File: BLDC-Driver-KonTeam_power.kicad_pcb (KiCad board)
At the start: 2 copper layers, 170 x 98.5 mm, 66 parts, among them J1 HOA_Enable, J10 HOB_Enable, J11 LOB_Enable, J12 A, J13 B, J14 C, J2 BUck, J3 Logic_Conn, J4 Logic_Test, J6 IN, J7 LOC_Enable, J8 HOC_Enable, J9 LOA_Enable, Q1 IRFZ44N, Q11 IRFZ44N, Q3 IRFZ44N, Q5 IRFZ44N, Q7 IRFZ44N, Q9 IRFZ44N, U1 IR2101, U2 IR2101, U3 IR2101, U4 LM7805_TO220

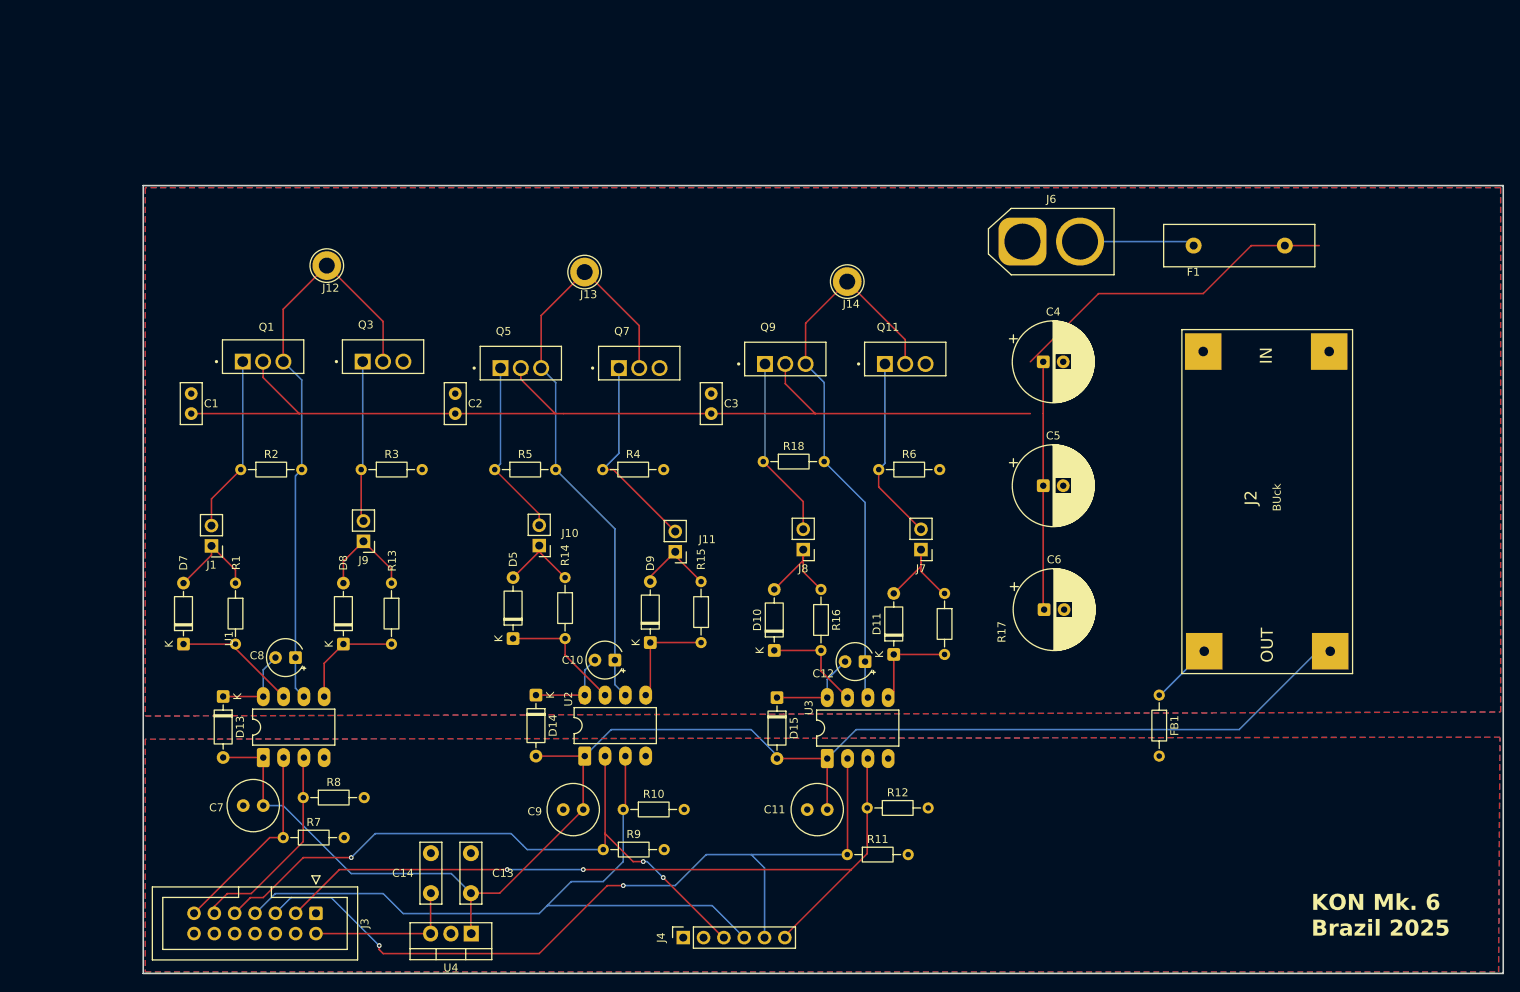
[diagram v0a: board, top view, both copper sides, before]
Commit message: - Added Footprint Buck converter - Add TVS diode for over voltage protection - Routed tracks (need confirmation) - Add conector for the horn, need to add specific connector - Added .step format for the mecanical considerations
Todo:
- add holes to fix to the car structure
- Make specific connector for the horn
- Calculate heatsink spacing
- Investigate about RC snubbers
- Investigate about the fly back diode efficency in the new mosfet
- Make the proyect has the embebed libraries for buck converter, mosfets, 
- Add Documentation Folder. (Datasheets, comparation sheets , etc)
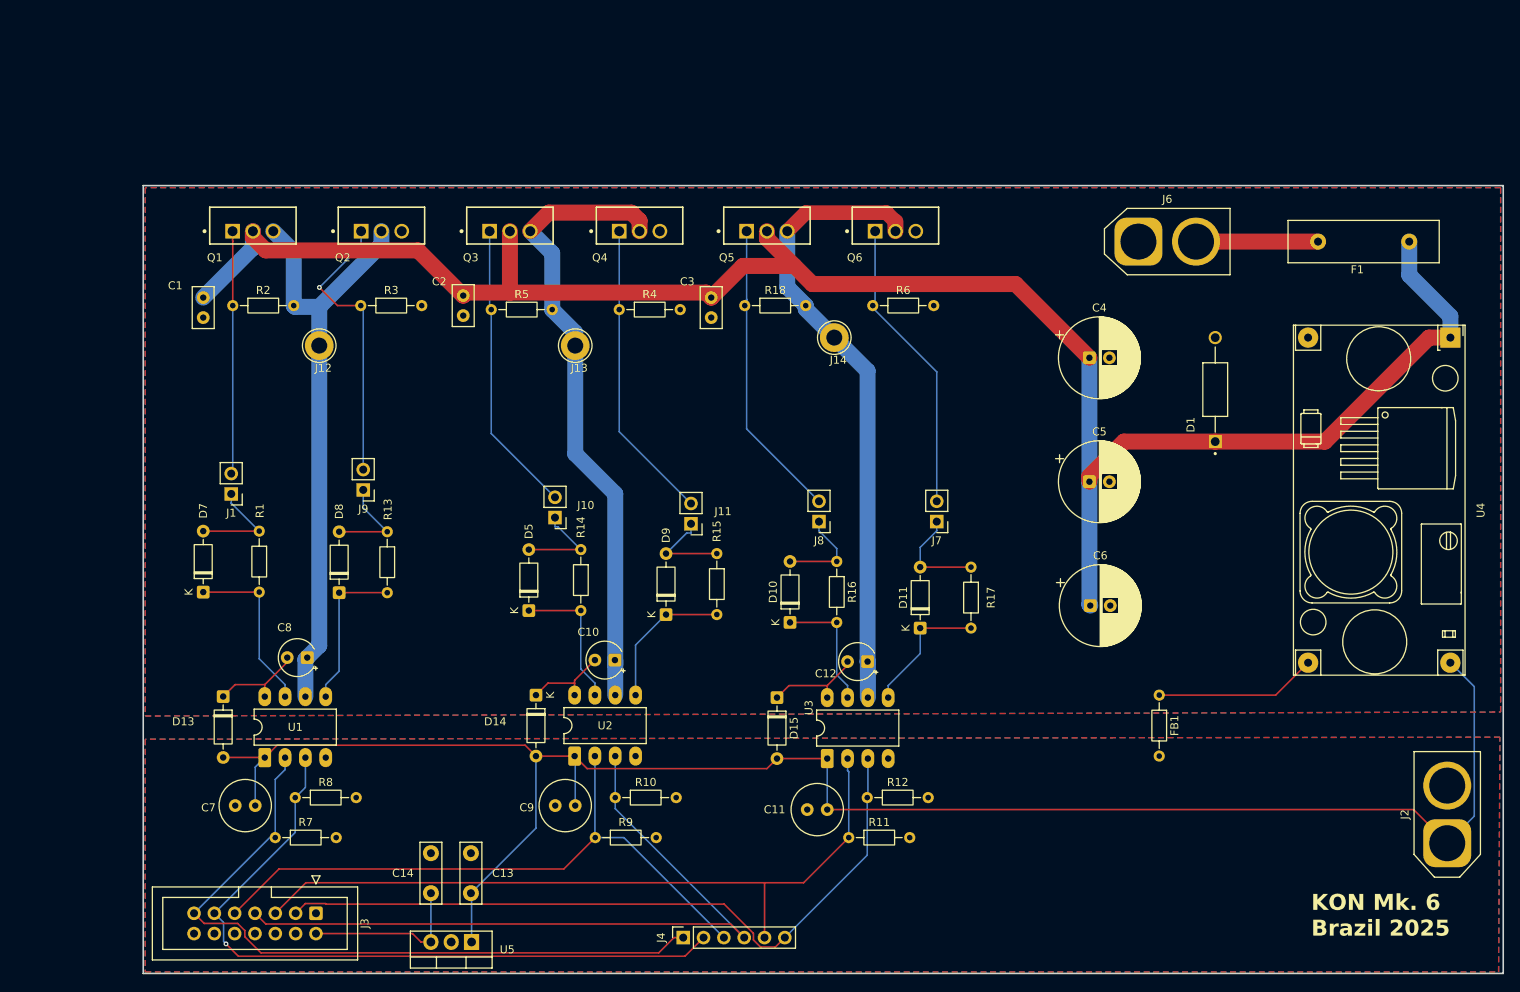
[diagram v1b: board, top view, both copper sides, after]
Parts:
- removed Q11, Q7, Q9: IRFZ44N, IRFZ44N:TO254P1016X419X2286-3
- added D1: P6KE68A, P6KE68A:DIOAD1300W80L670D310, F.Cu at (194.0, 72.0)
- added Q2: IRFB7730, kicad:IRFB7730, F.Cu at (89.8, 52.2)
- added Q4: IRFB7730, kicad:IRFB7730, F.Cu at (122.0, 52.2)
- added Q6: IRFB7730, kicad:IRFB7730, F.Cu at (154.0, 52.2)
- added U5: LM7805_TO220, Package_TO_SOT_THT:TO-220-3_Vertical, F.Cu at (101.0, 141.1)
- FB1: value FerriteBead_Small -> FerriteBead
- J2: value BUck -> Horn; footprint DC_DC_LM2596_small:DC_DC_LM2596_small -> Connector_AMASS:AMASS_XT60-F_1x02_P7.20mm_Vertical
- Q1, Q3, Q5: value IRFZ44N -> IRFB7730; footprint IRFZ44N:TO254P1016X419X2286-3 -> kicad:IRFB7730
- U4: value LM7805_TO220 -> Buck Converter; footprint Package_TO_SOT_THT:TO-220-3_Vertical -> KiCad:YAAJ_DCDC_StepDown_LM2596
- moved U4 143.3 mm to (223.4, 65.5), turned to -90 degrees
- moved J2 49.0 mm to (223.0, 128.7), turned to 90 degrees
- moved Q5 35.2 mm to (138.0, 52.2), turned to 90 degrees
- moved Q3 22.7 mm to (105.8, 52.2), turned to 90 degrees
- moved R2 20.5 mm to (71.2, 61.5)
- moved R6 20.5 mm to (151.2, 61.5)
- moved R3 20.5 mm to (87.2, 61.5)
- moved R4 20.1 mm to (119.5, 62.0)
- moved R5 20.0 mm to (103.5, 62.0)
- moved R18 19.6 mm to (135.2, 61.5)
- moved Q1 16.3 mm to (73.7, 52.2), turned to 90 degrees
- moved F1 15.6 mm to (218.2, 53.5)
- moved J6 14.5 mm to (184.4, 53.5)
- moved J12 10.0 mm to (82.0, 66.5)
- moved C2 9.80 mm to (100.0, 62.8), turned to 90 degrees
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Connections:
- net Net-(J6-Pin_2) renamed /Vin
- FB1 pad 1: Net-(J2-Pin_4) -> Net-(FB1-Pad1)
- J2 pad 1: VCC -> +12V
- J2 pad 2: GND -> Earth
- Q3 pad 1: LO_A -> HO_B
- Q3 pad 2: MA -> VCC
- Q3 pad 3: GND -> MB
- Q5 pad 1: HO_B -> HO_C
- Q5 pad 3: MB -> MC
- U4 pad 1: +12V -> VCC
- U4 pad 2: Earth -> GND
- U4 pad 3: +5V -> Net-(FB1-Pad1)
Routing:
- net /LIN_A: track 25.9 -> 89.9 mm, vias 0 -> 1
- net /HIN_A: track 25.1 -> 89.0 mm
- net +12V: track 185.1 -> 228.1 mm
- net VCC: track 204.4 -> 237.6 mm
- net Net-(FB1-Pad1): track 0.00 -> 20.3 mm
- net LO_A: track 20.1 -> 35.9 mm, vias 0 -> 1
- net HO_C: track 22.8 -> 38.4 mm
- net LO_C: track 23.2 -> 37.7 mm
- net HO_B: track 22.3 -> 36.6 mm
- net LO_B: track 25.8 -> 37.8 mm
- net /HIN_C: track 103.7 -> 92.4 mm, vias 2 -> 0
- net HO_A: track 22.1 -> 30.4 mm
- net MC: track 70.7 -> 78.6 mm
- net Net-(J2-Pin_4): track 7.90 -> 0.00 mm
- net /LIN_C: track 98.4 -> 91.6 mm, vias 2 -> 0
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
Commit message: cambio de driver, cambio de mosfet , añadido aislamiento galvanico entre logica y potencia
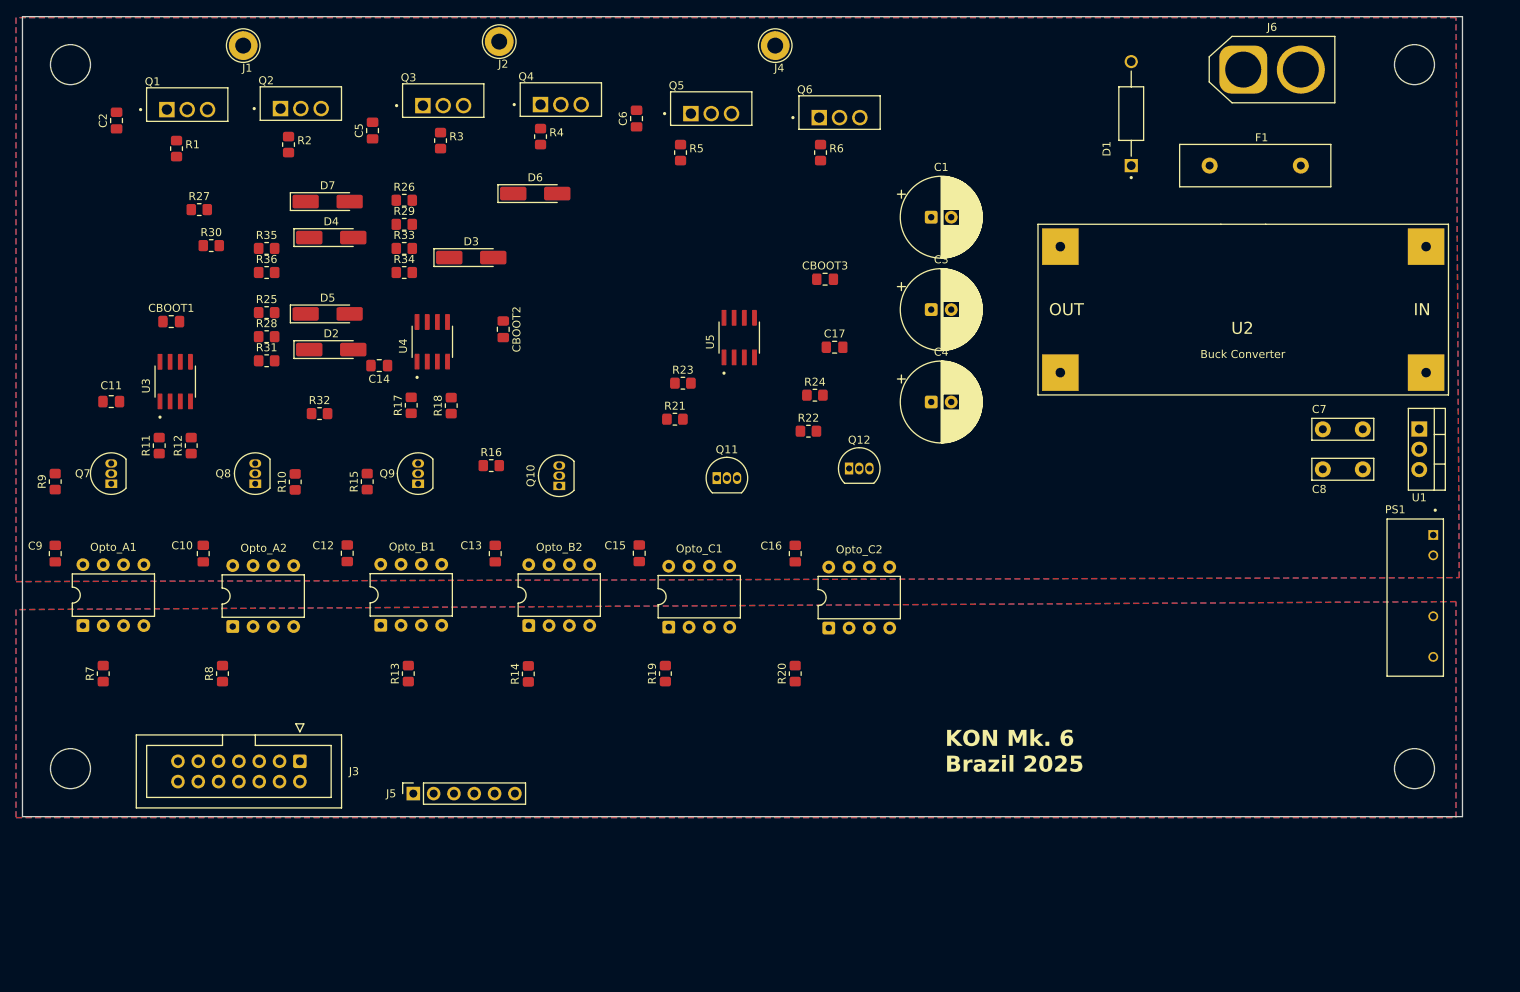
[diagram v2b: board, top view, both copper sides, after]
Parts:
- removed D10, D11, D13, D14, D15, D8, D9: SR560, Diode_THT:D_DO-35_SOD27_P7.62mm_Horizontal
- removed FB1: FerriteBead, Resistor_THT:R_Axial_DIN0204_L3.6mm_D1.6mm_P7.62mm_Horizontal
- removed J10: HOB_Enable, Connector_PinHeader_2.54mm:PinHeader_1x02_P2.54mm_Vertical
- removed J11: LOB_Enable, Connector_PinHeader_2.54mm:PinHeader_1x02_P2.54mm_Vertical
- removed J12: A, TestPoint:TestPoint_Loop_D3.80mm_Drill2.0mm
- removed J13: B, TestPoint:TestPoint_Loop_D3.80mm_Drill2.0mm
- removed J14: C, TestPoint:TestPoint_Loop_D3.80mm_Drill2.0mm
- removed J7: LOC_Enable, Connector_PinHeader_2.54mm:PinHeader_1x02_P2.54mm_Vertical
- removed J8: HOC_Enable, Connector_PinHeader_2.54mm:PinHeader_1x02_P2.54mm_Vertical
- removed J9: LOA_Enable, Connector_PinHeader_2.54mm:PinHeader_1x02_P2.54mm_Vertical
- added C15: 2.2uF, Capacitor_SMD:C_0805_2012Metric_Pad1.18x1.45mm_HandSolder, F.Cu at (122.0, 92.5)
- added C16: 2.2uF, Capacitor_SMD:C_0805_2012Metric_Pad1.18x1.45mm_HandSolder, F.Cu at (141.5, 92.5)
- added C17: 100uF, Capacitor_SMD:C_0805_2012Metric_Pad1.18x1.45mm_HandSolder, F.Cu at (146.4, 66.7)
- added CBOOT1: 6.8uF, Capacitor_SMD:C_0805_2012Metric_Pad1.18x1.45mm_HandSolder, F.Cu at (63.5, 63.5)
- added CBOOT2: 6.8uF, Capacitor_SMD:C_0805_2012Metric_Pad1.18x1.45mm_HandSolder, F.Cu at (105.0, 64.5)
- added CBOOT3: 6.8uF, Capacitor_SMD:C_0805_2012Metric_Pad1.18x1.45mm_HandSolder, F.Cu at (145.2, 58.2)
- added D2: LL4148, Diode_SMD:D_MiniMELF_Handsoldering, F.Cu at (83.5, 67.0)
- added D3: LL4148, Diode_SMD:D_MiniMELF_Handsoldering, F.Cu at (101.0, 55.5)
- added D4: LL4148, Diode_SMD:D_MiniMELF_Handsoldering, F.Cu at (83.5, 53.0)
- added D6: LL4148, Diode_SMD:D_MiniMELF_Handsoldering, F.Cu at (109.0, 47.5)
- added J5: Logic_Test, Connector_PinSocket_2.54mm:PinSocket_1x06_P2.54mm_Vertical, F.Cu at (93.8, 122.5)
- added Opto_A1: 6N137, Package_DIP:DIP-8_W7.62mm, F.Cu at (52.5, 101.5)
- added Opto_A2: 6N137, Package_DIP:DIP-8_W7.62mm, F.Cu at (71.2, 101.6)
- added Opto_B1: 6N137, Package_DIP:DIP-8_W7.62mm, F.Cu at (89.7, 101.5)
- added Opto_B2: 6N137, Package_DIP:DIP-8_W7.62mm, F.Cu at (108.2, 101.5)
- added Opto_C1: 6N137, Package_DIP:DIP-8_W7.62mm, F.Cu at (125.7, 101.7)
- added Opto_C2: 6N137, Package_DIP:DIP-8_W7.62mm, F.Cu at (145.7, 101.8)
- added PS1: RKZE-1205S_HP, KON:CONV_RKZE-1205S_HP, F.Cu at (219.0, 98.0)
- added Q10: 2N7000, Package_TO_SOT_THT:TO-92_Inline, F.Cu at (112.0, 84.0)
- added Q11: 2N7000, Package_TO_SOT_THT:TO-92_Inline, F.Cu at (131.7, 83.1)
- added Q12: 2N7000, Package_TO_SOT_THT:TO-92_Inline, F.Cu at (148.2, 81.9)
- added Q7: 2N7000, Package_TO_SOT_THT:TO-92_Inline, F.Cu at (56.0, 83.8)
- added Q8: 2N7000, Package_TO_SOT_THT:TO-92_Inline, F.Cu at (74.0, 83.8)
- added Q9: 2N7000, Package_TO_SOT_THT:TO-92_Inline, F.Cu at (94.4, 83.8)
- added R19: 100, Resistor_SMD:R_0805_2012Metric_Pad1.20x1.40mm_HandSolder, F.Cu at (125.3, 107.5)
- added R20: 100, Resistor_SMD:R_0805_2012Metric_Pad1.20x1.40mm_HandSolder, F.Cu at (141.5, 107.5)
- added R21: 2.2K, Resistor_SMD:R_0805_2012Metric_Pad1.20x1.40mm_HandSolder, F.Cu at (126.5, 75.7)
- added R22: 2.2K, Resistor_SMD:R_0805_2012Metric_Pad1.20x1.40mm_HandSolder, F.Cu at (143.2, 77.2)
- added R23: 1.2K, Resistor_SMD:R_0805_2012Metric_Pad1.20x1.40mm_HandSolder, F.Cu at (127.5, 71.2)
- added R24: 1.2K, Resistor_SMD:R_0805_2012Metric_Pad1.20x1.40mm_HandSolder, F.Cu at (144.0, 72.7)
- added R25: 1.2K, Resistor_SMD:R_0805_2012Metric_Pad1.20x1.40mm_HandSolder, F.Cu at (75.4, 62.4)
- added R26: 1.2K, Resistor_SMD:R_0805_2012Metric_Pad1.20x1.40mm_HandSolder, F.Cu at (92.6, 48.3)
- added R27: 1.2K, Resistor_SMD:R_0805_2012Metric_Pad1.20x1.40mm_HandSolder, F.Cu at (67.0, 49.5)
- added R28: 1.2K, Resistor_SMD:R_0805_2012Metric_Pad1.20x1.40mm_HandSolder, F.Cu at (75.4, 65.4)
- added R29: 1.2K, Resistor_SMD:R_0805_2012Metric_Pad1.20x1.40mm_HandSolder, F.Cu at (92.6, 51.3)
- added R30: 1.2K, Resistor_SMD:R_0805_2012Metric_Pad1.20x1.40mm_HandSolder, F.Cu at (68.5, 54.0)
- added R31: 1.2K, Resistor_SMD:R_0805_2012Metric_Pad1.20x1.40mm_HandSolder, F.Cu at (75.4, 68.4)
- added R32: 1.2K, Resistor_SMD:R_0805_2012Metric_Pad1.20x1.40mm_HandSolder, F.Cu at (82.0, 75.0)
- added R33: 1.2K, Resistor_SMD:R_0805_2012Metric_Pad1.20x1.40mm_HandSolder, F.Cu at (92.6, 54.4)
- added R34: 1.2K, Resistor_SMD:R_0805_2012Metric_Pad1.20x1.40mm_HandSolder, F.Cu at (92.6, 57.4)
- added R35: 1.2K, Resistor_SMD:R_0805_2012Metric_Pad1.20x1.40mm_HandSolder, F.Cu at (75.4, 54.4)
- added R36: 1.2K, Resistor_SMD:R_0805_2012Metric_Pad1.20x1.40mm_HandSolder, F.Cu at (75.4, 57.4)
- C1, C3: value 2.2uF -> 220uF 100V; footprint Capacitor_THT:C_Disc_D5.0mm_W2.5mm_P2.50mm -> Capacitor_THT:CP_Radial_D10.0mm_P2.50mm
- C10, C12: value 6.8uF -> 2.2uF; footprint Capacitor_THT:CP_Radial_Tantal_D4.5mm_P2.50mm -> Capacitor_SMD:C_0805_2012Metric_Pad1.18x1.45mm_HandSolder
- C11: footprint Capacitor_THT:C_Radial_D6.3mm_H11.0mm_P2.50mm -> Capacitor_SMD:C_0805_2012Metric_Pad1.18x1.45mm_HandSolder
- C13: value 0.1uF -> 2.2uF; footprint Capacitor_THT:C_Disc_D7.5mm_W2.5mm_P5.00mm -> Capacitor_SMD:C_0805_2012Metric_Pad1.18x1.45mm_HandSolder
- C14: value 0.33uF -> 100uF; footprint Capacitor_THT:C_Disc_D7.5mm_W2.5mm_P5.00mm -> Capacitor_SMD:C_0805_2012Metric_Pad1.18x1.45mm_HandSolder
- C2: footprint Capacitor_THT:C_Disc_D5.0mm_W2.5mm_P2.50mm -> Capacitor_SMD:C_0805_2012Metric_Pad1.18x1.45mm_HandSolder
- C5, C6: value 220uF 100V -> 2.2uF; footprint Capacitor_THT:CP_Radial_D10.0mm_P2.50mm -> Capacitor_SMD:C_0805_2012Metric_Pad1.18x1.45mm_HandSolder
- C7: value 100uF -> 0.1uF; footprint Capacitor_THT:C_Radial_D6.3mm_H11.0mm_P2.50mm -> Capacitor_THT:C_Disc_D7.5mm_W2.5mm_P5.00mm
- C8: value 6.8uF -> 0.33uF; footprint Capacitor_THT:CP_Radial_Tantal_D4.5mm_P2.50mm -> Capacitor_THT:C_Disc_D7.5mm_W2.5mm_P5.00mm
- C9: value 100uF -> 2.2uF; footprint Capacitor_THT:C_Radial_D6.3mm_H11.0mm_P2.50mm -> Capacitor_SMD:C_0805_2012Metric_Pad1.18x1.45mm_HandSolder
- D1: footprint P6KE68A:DIOAD1300W80L670D310 -> KON:DIOAD1300W80L670D310
- D5, D7: value SR560 -> LL4148; footprint Diode_THT:D_DO-35_SOD27_P7.62mm_Horizontal -> Diode_SMD:D_MiniMELF_Handsoldering
- J1: value HOA_Enable -> A; footprint Connector_PinHeader_2.54mm:PinHeader_1x02_P2.54mm_Vertical -> TestPoint:TestPoint_Loop_D3.80mm_Drill2.0mm
- J2: value Horn -> B; footprint Connector_AMASS:AMASS_XT60-F_1x02_P7.20mm_Vertical -> TestPoint:TestPoint_Loop_D3.80mm_Drill2.0mm
- J4: value Logic_Test -> C; footprint Connector_PinSocket_2.54mm:PinSocket_1x06_P2.54mm_Vertical -> TestPoint:TestPoint_Loop_D3.80mm_Drill2.0mm
- Q1, Q2, Q3, Q4, Q5, Q6: value IRFB7730 -> IRFB3607; footprint kicad:IRFB7730 -> KON:TO254P1016X419X2286-3
- R1: value 100 -> 10K; footprint Resistor_THT:R_Axial_DIN0204_L3.6mm_D1.6mm_P7.62mm_Horizontal -> Resistor_SMD:R_0805_2012Metric_Pad1.20x1.40mm_HandSolder
- R10, R9: value 10K -> 2.2K; footprint Resistor_THT:R_Axial_DIN0204_L3.6mm_D1.6mm_P7.62mm_Horizontal -> Resistor_SMD:R_0805_2012Metric_Pad1.20x1.40mm_HandSolder
- R11, R12, R18: value 10K -> 1.2K; footprint Resistor_THT:R_Axial_DIN0204_L3.6mm_D1.6mm_P7.62mm_Horizontal -> Resistor_SMD:R_0805_2012Metric_Pad1.20x1.40mm_HandSolder
- R13, R14, R2, R3, R4, R5, R6: footprint Resistor_THT:R_Axial_DIN0204_L3.6mm_D1.6mm_P7.62mm_Horizontal -> Resistor_SMD:R_0805_2012Metric_Pad1.20x1.40mm_HandSolder
- R15, R16: value 100 -> 2.2K; footprint Resistor_THT:R_Axial_DIN0204_L3.6mm_D1.6mm_P7.62mm_Horizontal -> Resistor_SMD:R_0805_2012Metric_Pad1.20x1.40mm_HandSolder
- R17: value 100 -> 1.2K; footprint Resistor_THT:R_Axial_DIN0204_L3.6mm_D1.6mm_P7.62mm_Horizontal -> Resistor_SMD:R_0805_2012Metric_Pad1.20x1.40mm_HandSolder
- R7, R8: value 10K -> 100; footprint Resistor_THT:R_Axial_DIN0204_L3.6mm_D1.6mm_P7.62mm_Horizontal -> Resistor_SMD:R_0805_2012Metric_Pad1.20x1.40mm_HandSolder
- U1: value IR2101 -> LM7805_TO220; footprint Package_DIP:DIP-8_W7.62mm_LongPads -> Package_TO_SOT_THT:TO-220-3_Vertical
- U2: value IR2101 -> Buck Converter; footprint Package_DIP:DIP-8_W7.62mm_LongPads -> KON:DC_DC_LM2596_small
- U3: value IR2101 -> L6387; footprint Package_DIP:DIP-8_W7.62mm_LongPads -> KON:SOIC127P600X175-8N
- U4: value Buck Converter -> L6387; footprint KiCad:YAAJ_DCDC_StepDown_LM2596 -> KON:SOIC127P600X175-8N
- U5: value LM7805_TO220 -> L6387; footprint Package_TO_SOT_THT:TO-220-3_Vertical -> KON:SOIC127P600X175-8N
- moved J2 155.2 mm to (104.5, 28.5), turned to 0 degrees
- moved U1 150.0 mm to (219.5, 76.9), turned to -90 degrees
- moved C7 146.2 mm to (212.4, 77.0)
- moved C8 134.0 mm to (212.4, 82.0)
- moved U4 127.3 mm to (96.1, 66.0), turned to 90 degrees
- moved J4 112.1 mm to (139.0, 29.0), turned to 0 degrees
- moved C11 103.0 mm to (56.0, 73.5)
- moved U2 100.5 mm to (197.5, 62.0), turned to 180 degrees
- moved C5 99.8 mm to (88.7, 39.6), turned to 90 degrees
- moved R11 99.1 mm to (62.0, 79.0), turned to 90 degrees
- moved R12 95.3 mm to (66.0, 79.0), turned to 90 degrees
- moved U3 94.1 mm to (64.0, 71.0)
- moved C1 91.9 mm to (158.5, 50.5), turned to 0 degrees
- moved C6 83.2 mm to (121.7, 38.1), turned to 90 degrees
- moved U5 82.6 mm to (134.5, 65.5), turned to 90 degrees
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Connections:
- C1 pad 1: GND -> VCC
- C1 pad 2: VCC -> GND
- C10 pad 1: MB -> +5V
- C10 pad 2: Net-(D14-K) -> GND
- C11 pad 2: Earth -> GND
- C12 pad 1: MC -> +5V
- C12 pad 2: Net-(D15-K) -> GND
- C13 pad 1: +12V -> +5V
- C13 pad 2: Earth -> GND
- C14 pad 1: +5V -> +12V
- C14 pad 2: Earth -> GND
- C3 pad 1: GND -> VCC
- C3 pad 2: VCC -> GND
- C5 pad 1: VCC -> GND
- C5 pad 2: GND -> VCC
- C6 pad 1: VCC -> GND
- C6 pad 2: GND -> VCC
- C7 pad 2: Earth -> GND
- C8 pad 1: MA -> +5V
- C8 pad 2: Net-(D13-K) -> GND
- C9 pad 1: +12V -> +5V
- C9 pad 2: Earth -> GND
- D5 pad 1: Net-(D5-K) -> /DriverA/Power_High
- D7 pad 1: Net-(D7-K) -> /DriverC/Power_High
- J1 pad 1: Net-(D7-A) -> MA
- J2 pad 1: +12V -> MB
- J3 pad 11: /LIN_A -> LIN_A
- J3 pad 13: /HIN_A -> HIN_A
- J3 pad 2: +5V -> +5VL
- J3 pad 3: /LIN_C -> LIN_C
- J3 pad 5: /HIN_C -> HIN_C
- J3 pad 7: /LIN_B -> LIN_B
- J3 pad 9: /HIN_B -> HIN_B
- J4 pad 1: /HIN_A -> MC
- R1 pad 1: Net-(D7-A) -> MA
- R1 pad 2: Net-(D7-K) -> HO_A
- R10 pad 1: /LIN_B -> +5V
- R10 pad 2: Earth -> Net-(Opto_A2-VO)
- R11 pad 1: /HIN_C -> +5V
- R11 pad 2: Earth -> /DriverA/Power_High
- R12 pad 1: /LIN_C -> +5V
- R12 pad 2: Earth -> /DriverA/Power_Low
- R13 pad 1: Net-(D8-A) -> HIN_B
- R13 pad 2: Net-(D8-K) -> Net-(Opto_B1-A)
- R14 pad 1: Net-(D5-A) -> LIN_B
- R14 pad 2: Net-(D5-K) -> Net-(Opto_B2-A)
- R15 pad 1: Net-(D9-A) -> +5V
- R15 pad 2: Net-(D9-K) -> Net-(Opto_B1-VO)
- R16 pad 1: Net-(D10-A) -> +5V
- R16 pad 2: Net-(D10-K) -> Net-(Opto_B2-VO)
- R17 pad 1: Net-(D11-A) -> +5V
- R17 pad 2: Net-(D11-K) -> /DriverB/Power_High
- R18 pad 1: HO_C -> +5V
- R18 pad 2: MC -> /DriverB/Power_Low
- R2 pad 1: HO_A -> GND
- R2 pad 2: MA -> LO_A
- R3 pad 1: LO_A -> MB
- R3 pad 2: GND -> HO_B
- R4 pad 1: LO_B -> GND
- R4 pad 2: GND -> LO_B
- R5 pad 1: HO_B -> MC
- R5 pad 2: MB -> HO_C
- R6 pad 1: LO_C -> GND
- R6 pad 2: GND -> LO_C
- R7 pad 1: /HIN_A -> HIN_A
- R7 pad 2: Earth -> Net-(Opto_A1-A)
- R8 pad 1: /LIN_A -> LIN_A
- R8 pad 2: Earth -> Net-(Opto_A2-A)
- R9 pad 1: /HIN_B -> +5V
- R9 pad 2: Earth -> Net-(Opto_A1-VO)
- U1 pad 2: /HIN_A -> Earth
- U1 pad 3: /LIN_A -> +5V
- U2 pad 1: +12V -> VCC
- U2 pad 2: /HIN_B -> GND
- U2 pad 3: /LIN_B -> GND
- U2 pad 4: Earth -> +12V
- U3 pad 2: /HIN_C -> Net-(U3-HIN)
- U3 pad 3: /LIN_C -> Net-(U3-LIN)
- U3 pad 4: Earth -> GND
- U3 pad 5: Net-(D11-K) -> LO_A
- U3 pad 6: MC -> MA
- U3 pad 7: Net-(D10-K) -> HO_A
- U3 pad 8: Net-(D15-K) -> Net-(U3-VB)
- U4 pad 1: VCC -> +12V
- U4 pad 2: GND -> Net-(U4-HIN)
- U4 pad 4: +12V -> GND
- U5 pad 2: Earth -> Net-(U5-HIN)
- U5 pad 3: +5V -> Net-(U5-LIN)
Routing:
- net VCC: track 237.6 -> 0.00 mm
- net +12V: track 228.1 -> 0.00 mm
- net /HIN_C: track 92.4 -> 0.00 mm
- net /LIN_B: track 91.8 -> 0.00 mm
- net /LIN_C: track 91.6 -> 0.00 mm
- net /LIN_A: track 89.9 -> 0.00 mm, vias 1 -> 0
- net /HIN_A: track 89.0 -> 0.00 mm
- net /HIN_B: track 80.5 -> 0.00 mm
- net MB: track 79.3 -> 0.00 mm
- net MC: track 78.6 -> 0.00 mm
- net MA: track 75.7 -> 0.00 mm
- net HO_C: track 38.4 -> 0.00 mm
- net LO_B: track 37.8 -> 0.00 mm
- net LO_C: track 37.7 -> 0.00 mm
- net HO_B: track 36.6 -> 0.00 mm
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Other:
- board size 170 x 98.5 mm -> 180 x 100 mm
